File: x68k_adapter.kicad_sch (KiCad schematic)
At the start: 29 parts, among them J1 USB_A, J2 USB_A, J3 SWD, J4 UART, J5 X68k conn, SW1 SW_Push, U1 PGA2040, U2 USB2422, U3 TPD2EUSB30, U4 TPD2EUSB30, Y1 24MHz

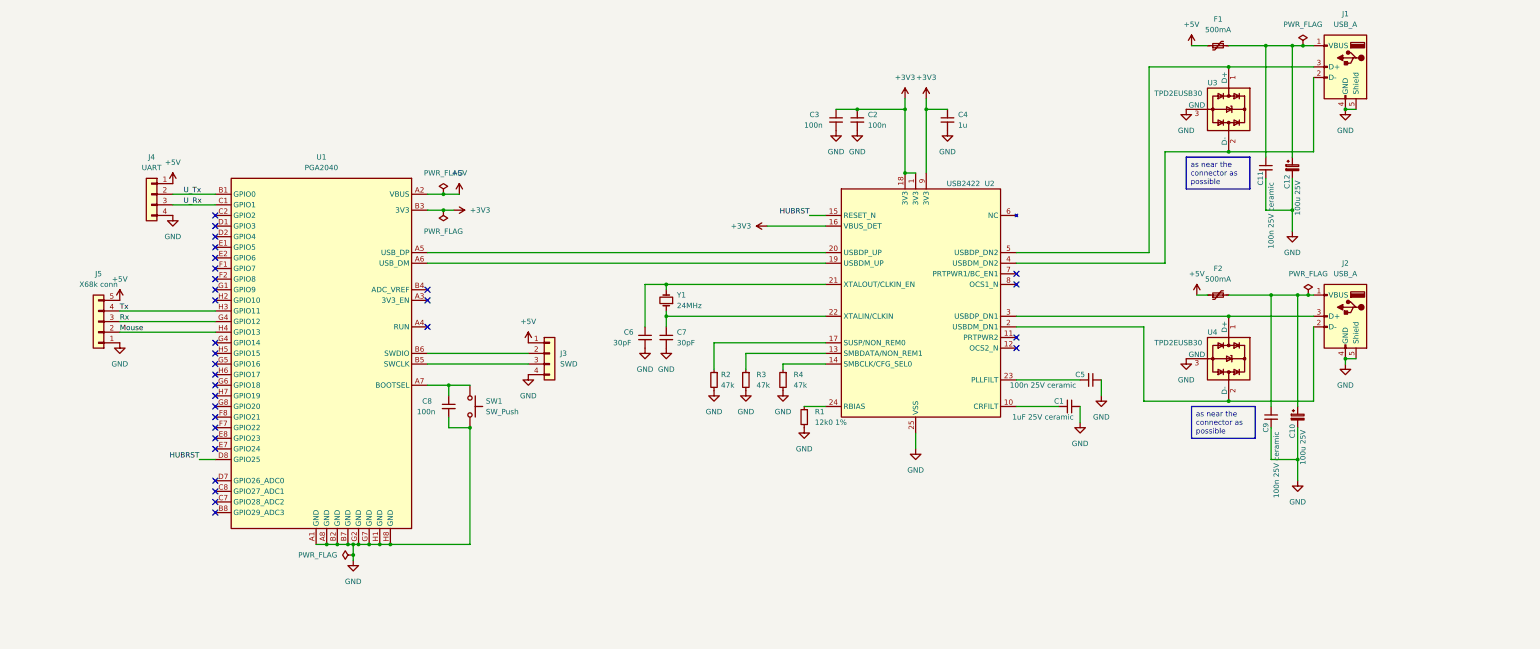
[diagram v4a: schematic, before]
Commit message: Add LCD and finish USB DPs
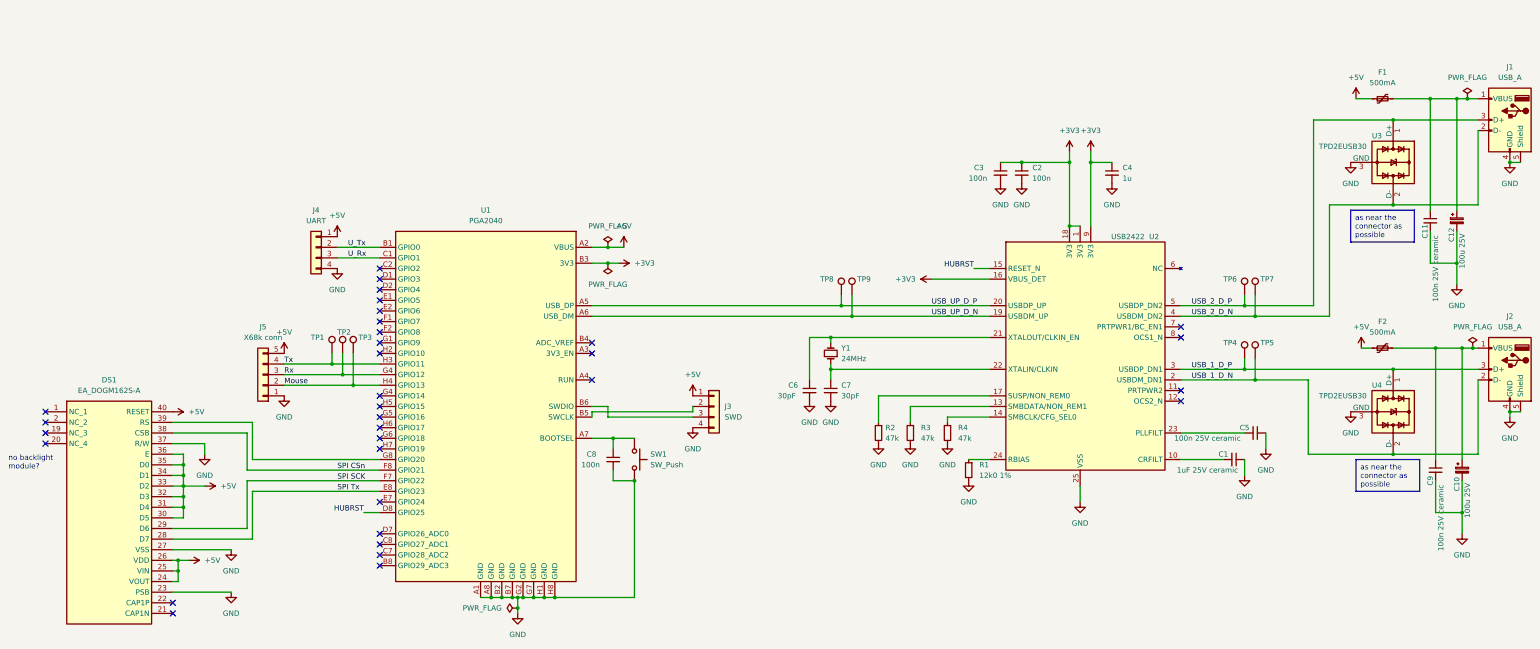
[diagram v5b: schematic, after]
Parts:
- added DS1: EA_DOGM162S-A, Display:EA_DOGM128-6, symbol LCD EA_DOGM:EA_DOGM162S-A
- added TP1, TP2, TP3, TP4, TP5, TP6, TP7, TP8, TP9: TestPoint, TestPoint:TestPoint_Pad_1.0x1.0mm, symbol Connector:TestPoint
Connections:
- net +5V: now also DS1.24 (VOUT), DS1.25 (VIN), DS1.26 (VDD), DS1.30 (D5), DS1.31 (D4), DS1.32 (D3), DS1.33 (D2), DS1.34 (D1), DS1.35 (D0), DS1.36 (E), DS1.40 (RESET)
- net GND: now also DS1.23 (PSB), DS1.27 (VSS), DS1.37 (R/W)
- net Mouse: now also TP3.1
- net Rx: now also TP2.1
- net Tx: now also TP1.1
- net USB_1_D_N: now reaches J2.2 (D-), U2.2 (USBDM_DN1), U4.2 (D-)
- net USB_1_D_N: now also TP5.1
- net USB_1_D_P: now reaches J2.3 (D+), U2.3 (USBDP_DN1), U4.1 (D+)
- net USB_1_D_P: now also TP4.1
- net at J3.2 (Pin_2): now also U1.B5 (SWCLK); no longer U1.B6 (SWDIO)
- net at J3.3 (Pin_3): now also U1.B6 (SWDIO); no longer U1.B5 (SWCLK)
- net USB_UP_D_P: now reaches U1.A5 (USB_DP), U2.20 (USBDP_UP)
- net USB_UP_D_P: now also TP8.1
- net USB_UP_D_N: now reaches U1.A6 (USB_DM), U2.19 (USBDM_UP)
- net USB_UP_D_N: now also TP9.1
- net SPI Tx: now reaches U1.E8 (GPIO23)
- net SPI Tx: now also DS1.28 (D7)
- net SPI SCK: now reaches U1.F7 (GPIO22)
- net SPI SCK: now also DS1.29 (D6)
- net SPI CSn: now reaches U1.F8 (GPIO21)
- net SPI CSn: now also DS1.38 (CSB)
- net at U1.G8 (GPIO20): now also DS1.39 (RS)
- net USB_2_D_N: now reaches J1.2 (D-), U2.4 (USBDM_DN2), U3.2 (D-)
- net USB_2_D_N: now also TP7.1
- net USB_2_D_P: now reaches J1.3 (D+), U2.5 (USBDP_DN2), U3.1 (D+)
- net USB_2_D_P: now also TP6.1
- no-connect marks 31 -> 33
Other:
- note added: "no backlight module?"
- moved on the sheet: C1, C10, C11, C12, C2, C3, C4, C5, C6, C7, C8, C9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
